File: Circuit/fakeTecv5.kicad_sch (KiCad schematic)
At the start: 76 parts, among them J1 EXTRA, J11 FET1 3,3, J12 FET2 3,3, J13 FET3 3,3, J14 GPS Pins, J16 Encoder Pads, J37 SCL, J38 JST-SH-4, J39 SDA, J40 3.3V, J41 GND, J42 FET1, J43 FET2, J44 FET3, J45 GND, J46 3.3V, J47 GND, J48 GND, J49 GND, J5 I2C Oled screen, J50 3.3V, J51 GND, J52 GND, J6 FET1 Drain, J7 FET2 Drain, J8 FET3 Drain, J9 JST-PH-2, M1 ERM Motor, Q1 AO3400A, Q2 AO3400A, Q3 AO3400A, SW1 Reset, SW2 SW_Push, SW3 RotaryEncoder_Switch, U1 XB8089D0, U2 HT-RA62, U3 nice!nano v2

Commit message: use alignment hole
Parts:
- U3: footprint faketec:NICE!NANO and pro-micro V2_2 SMD -> faketec:NICE!NANO and pro-micro V2_2 SMD_With_Alignment_Holes
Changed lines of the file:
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@@
 			)
 		)
-		(property "Footprint" "faketec:NICE!NANO and pro-micro V2_2 SMD"
+		(property "Footprint" "faketec:NICE!NANO and pro-micro V2_2 SMD_With_Alignment_Holes"
 			(at 124.46 82.55 0)
 			(effects

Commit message: adjust extra testpoint to the side of oled screen
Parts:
- J5: footprint Connector_PinHeader_2.54mm:PinHeader_1x04_P2.54mm_Vertical -> faketec:OLED_PinHeader_1x04_P2.54mm_Vertical
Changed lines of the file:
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@@
 			)
 		)
-		(property "Footprint" "Connector_PinHeader_2.54mm:PinHeader_1x04_P2.54mm_Vertical"
+		(property "Footprint" "faketec:OLED_PinHeader_1x04_P2.54mm_Vertical"
 			(at 179.07 30.48 0)
 			(effects

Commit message: hw: modify power connector to support both JST GH and PH connector
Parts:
- J9: footprint Connector_JST:JST_PH_S2B-PH-SM4-TB_1x02-1MP_P2.00mm_Horizontal -> faketec:JST_PH_S2B-PH-SM4-TB_1x02-1MP_P2.00mm_Horizontal
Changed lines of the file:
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@@
 			)
 		)
-		(property "Footprint" "Connector_JST:JST_PH_S2B-PH-SM4-TB_1x02-1MP_P2.00mm_Horizontal"
+		(property "Footprint" "faketec:JST_PH_S2B-PH-SM4-TB_1x02-1MP_P2.00mm_Horizontal"
 			(at 24.13 110.49 0)
 			(effects

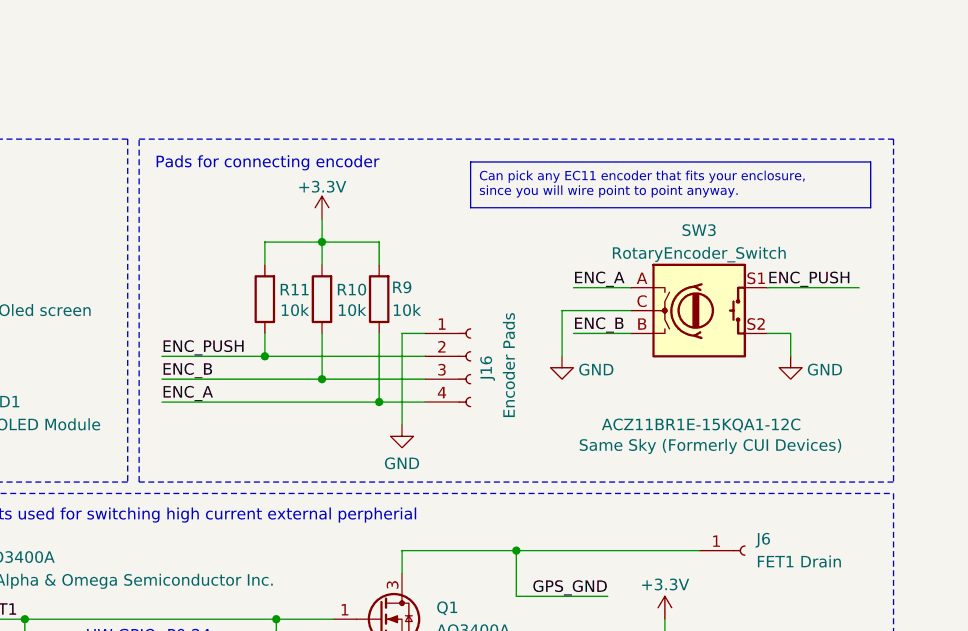
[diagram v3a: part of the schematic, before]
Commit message: hw: refactor spi routing. Make OLED screen pins friction fit
SPI is likely running under 50mHz mark so vias is not an issue and want to keep signal path small. Made careful note to keep all spi lines under the ground plane as much as possible.
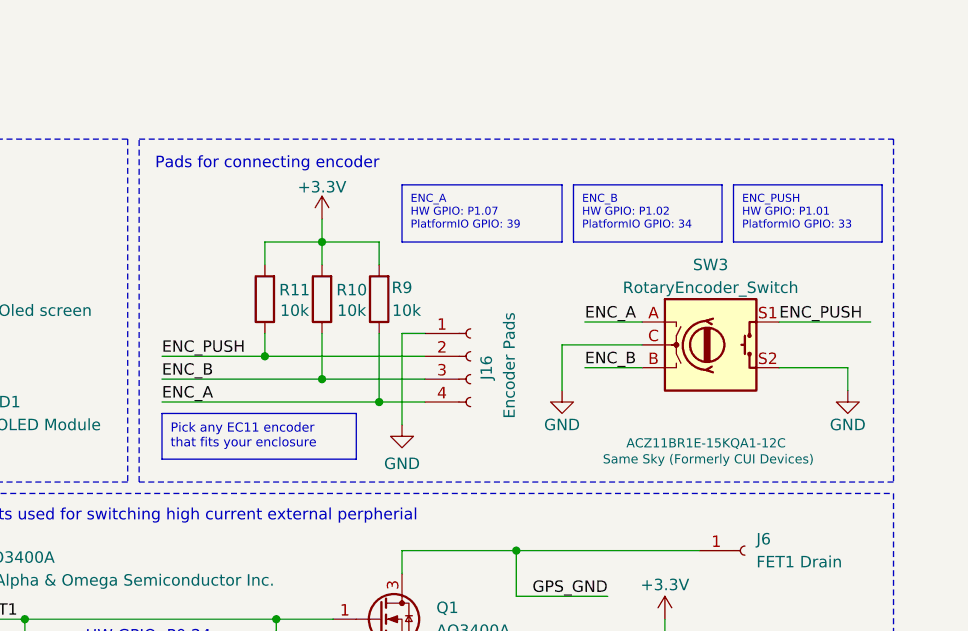
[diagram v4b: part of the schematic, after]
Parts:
- J5: footprint faketec:OLED_PinHeader_1x04_P2.54mm_Vertical -> faketec:OLED_PinHeader_1x04_P2.54mm_Vertical_Friction_Fit
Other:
- moved on the sheet: SW3
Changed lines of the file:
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@@
 		)
 	)
+	(text_box "ENC_B\nHW GPIO: P1.02\nPlatformIO GPIO: 34"
+		(exclude_from_sim no)
+		(at 247.65 19.05 0)
+		(size 16.51 6.35)
+		(margins 0.9525 0.9525 0.9525 0.9525)
+		(stroke
+			(width 0)
+			(type solid)
+		)
+		(fill
+			(type none)
+		)
+		(effects
+			(font
+				(size 0.889 0.889)
+			)
+			(justify left top)
+		)
+	)
+	(text_box "ENC_A\nHW GPIO: P1.07\nPlatformIO GPIO: 39"
+		(exclude_from_sim no)
+		(at 228.6 19.05 0)
+		(size 17.78 6.35)
+		(margins 0.9525 0.9525 0.9525 0.9525)
+		(stroke
+			(width 0)
+			(type solid)
+		)
+		(fill
+			(type none)
+		)
+		(effects
+			(font
+				(size 0.889 0.889)
+			)
+			(justify left top)
+		)
+	)
+	(text_box "ENC_PUSH\nHW GPIO: P1.01\nPlatformIO GPIO: 33"
+		(exclude_from_sim no)
+		(at 265.43 19.05 0)
+		(size 16.51 6.35)
+		(margins 0.9525 0.9525 0.9525 0.9525)
+		(stroke
+			(width 0)
+			(type solid)
+		)
+		(fill
+			(type none)
+		)
+		(effects
+			(font
+				(size 0.889 0.889)
+			)
+			(justify left top)
+		)
+	)
 	(text_box "Alternatively can use SI2312 (More expensive. Higher current)"
 		(exclude_from_sim no)
@@
 		)
 	)
-	(text_box "Can pick any EC11 encoder that fits your enclosure,\nsince you will wire point to point anyway."
+	(text_box "Pick any EC11 encoder that fits your enclosure"
 		(exclude_from_sim no)
-		(at 236.22 16.51 0)
-		(size 44.45 5.08)
+		(at 201.93 44.45 0)
+		(size 21.59 5.08)
 		(margins 0.9525 0.9525 0.9525 0.9525)
 		(stroke
@@
 	(wire
 		(pts
-			(xy 246.38 33.02) (xy 246.38 38.1)
+			(xy 246.38 36.83) (xy 246.38 41.91)
 		)
 		(stroke
@@
 	(wire
 		(pts
-			(xy 269.24 30.48) (xy 279.4 30.48)
+			(xy 270.51 34.29) (xy 280.67 34.29)
 		)
 		(stroke
@@
 	(wire
 		(pts
-			(xy 254 33.02) (xy 246.38 33.02)
+			(xy 255.27 36.83) (xy 246.38 36.83)
 		)
 		(stroke
@@
 	(wire
 		(pts
-			(xy 269.24 35.56) (xy 271.78 35.56)
+			(xy 270.51 39.37) (xy 278.13 39.37)
 		)
 		(stroke
@@
 	(wire
 		(pts
-			(xy 271.78 35.56) (xy 271.78 38.1)
+			(xy 278.13 39.37) (xy 278.13 41.91)
 		)
 		(stroke
@@
 	(wire
 		(pts
-			(xy 247.65 35.56) (xy 254 35.56)
+			(xy 248.92 39.37) (xy 255.27 39.37)
 		)
 		(stroke
@@
 	(wire
 		(pts
-			(xy 247.65 30.48) (xy 254 30.48)
+			(xy 248.92 34.29) (xy 255.27 34.29)
 		)
 		(stroke
@@
 	)
 	(label "ENC_A"
-		(at 247.65 30.48 0)
+		(at 248.92 34.29 0)
 		(effects
 			(font
@@
 	)
 	(label "ENC_PUSH"
-		(at 269.24 30.48 0)
+		(at 270.51 34.29 0)
 		(effects
 			(font
@@
 	)
 	(label "ENC_B"
-		(at 247.65 35.56 0)
+		(at 248.92 39.37 0)
 		(effects
 			(font
@@
 	(symbol
 		(lib_id "power:GND")
-		(at 246.38 38.1 0)
+		(at 246.38 41.91 0)
 		(unit 1)
 		(exclude_from_sim no)
@@
 		(dnp no)
 		(property "Reference" "#PWR09"
-			(at 246.38 44.45 0)
+			(at 246.38 48.26 0)
 			(effects
 				(font
@@
 		)
 		(property "Value" "GND"
-			(at 250.19 39.624 0)
+			(at 246.38 45.72 0)
 			(effects
 				(font
@@
 		)
 		(property "Footprint" ""
-			(at 246.38 38.1 0)
+			(at 246.38 41.91 0)
 			(effects
 				(font
@@
 		)
 		(property "Datasheet" ""
-			(at 246.38 38.1 0)
+			(at 246.38 41.91 0)
 			(effects
 				(font
@@
 		)
 		(property "Description" "Power symbol creates a global label with name \"GND\" , ground"
-			(at 246.38 38.1 0)
+			(at 246.38 41.91 0)
 			(effects
 				(font
@@
 	(symbol
 		(lib_id "Device:RotaryEncoder_Switch")
-		(at 261.62 33.02 0)
+		(at 262.89 36.83 0)
 		(unit 1)
 		(exclude_from_sim yes)
@@
 		(dnp no)
 		(property "Reference" "SW3"
-			(at 261.62 24.13 0)
+			(at 262.89 27.94 0)
 			(effects
 				(font
@@
 		)
 		(property "Value" "RotaryEncoder_Switch"
-			(at 261.62 26.67 0)
+			(at 262.89 30.48 0)
 			(effects
 				(font
@@
 		)
 		(property "Footprint" ""
-			(at 257.81 28.956 0)
+			(at 259.08 32.766 0)
 			(effects
 				(font
@@
 		)
 		(property "Datasheet" "https://www.cuidevices.com/product/resource/acz11.pdf"
-			(at 261.62 26.416 0)
+			(at 262.89 30.226 0)
 			(effects
 				(font
@@
 		)
 		(property "Description" "Rotary encoder, dual channel, incremental quadrate outputs, with switch"
-			(at 261.62 33.02 0)
+			(at 262.89 36.83 0)
 			(effects
 				(font
@@
 		)
 		(property "MPD" "EC11 horizontal rotary encoder Plum blossom shaft With switch 15/20mm 5PIN 20bit pulse digital potentiometer With knob cap"
-			(at 261.62 33.02 0)
+			(at 262.89 36.83 0)
 			(effects
 				(font
@@
 		)
 		(property "MPL" "https://www.aliexpress.com/item/1005010398201852.html or https://www.digikey.com.au/en/products/detail/same-sky-formerly-cui-devices/ACZ11BR1E-15KQA1-12C/1923334"
-			(at 261.62 33.02 0)
+			(at 262.89 36.83 0)
 			(effects
 				(font
@@
 		)
 		(property "Shopping" "https://www.aliexpress.com/w/wholesale-rotary-encoder-EC11-horizontal.html or https://www.digikey.com.au/short/7v5m7j9j"
-			(at 261.62 33.02 0)
+			(at 262.89 36.83 0)
 			(effects
 				(font
@@
 		)
 		(property "MPN" "ACZ11BR1E-15KQA1-12C"
-			(at 261.874 45.72 0)
+			(at 262.382 47.752 0)
 			(effects
 				(font
-					(size 1.27 1.27)
+					(size 1.016 1.016)
 				)
 			)
 		)
 		(property "Manufacturer" "Same Sky (Formerly CUI Devices)"
-			(at 262.89 48.006 0)
+			(at 262.636 49.53 0)
 			(effects
 				(font
-					(size 1.27 1.27)
+					(size 1.016 1.016)
 				)
 			)
 		)
 		(property "Package" "EC11"
-			(at 261.62 33.02 0)
+			(at 262.89 36.83 0)
 			(effects
 				(font
@@
 	(symbol
 		(lib_id "power:GND")
-		(at 271.78 38.1 0)
+		(at 278.13 41.91 0)
 		(unit 1)
 		(exclude_from_sim no)
@@
 		(dnp no)
 		(property "Reference" "#PWR047"
-			(at 271.78 44.45 0)
+			(at 278.13 48.26 0)
 			(effects
 				(font
@@
 		)
 		(property "Value" "GND"
-			(at 275.59 39.624 0)
+			(at 278.13 45.72 0)
 			(effects
 				(font
@@
 		)
 		(property "Footprint" ""
-			(at 271.78 38.1 0)
+			(at 278.13 41.91 0)
 			(effects
 				(font
@@
 		)
 		(property "Datasheet" ""
-			(at 271.78 38.1 0)
+			(at 278.13 41.91 0)
 			(effects
 				(font
@@
 		)
 		(property "Description" "Power symbol creates a global label with name \"GND\" , ground"
-			(at 271.78 38.1 0)
+			(at 278.13 41.91 0)
 			(effects
 				(font
@@
 			)
 		)
-		(property "Footprint" "faketec:OLED_PinHeader_1x04_P2.54mm_Vertical"
+		(property "Footprint" "faketec:OLED_PinHeader_1x04_P2.54mm_Vertical_Friction_Fit"
 			(at 179.07 30.48 0)
 			(effects

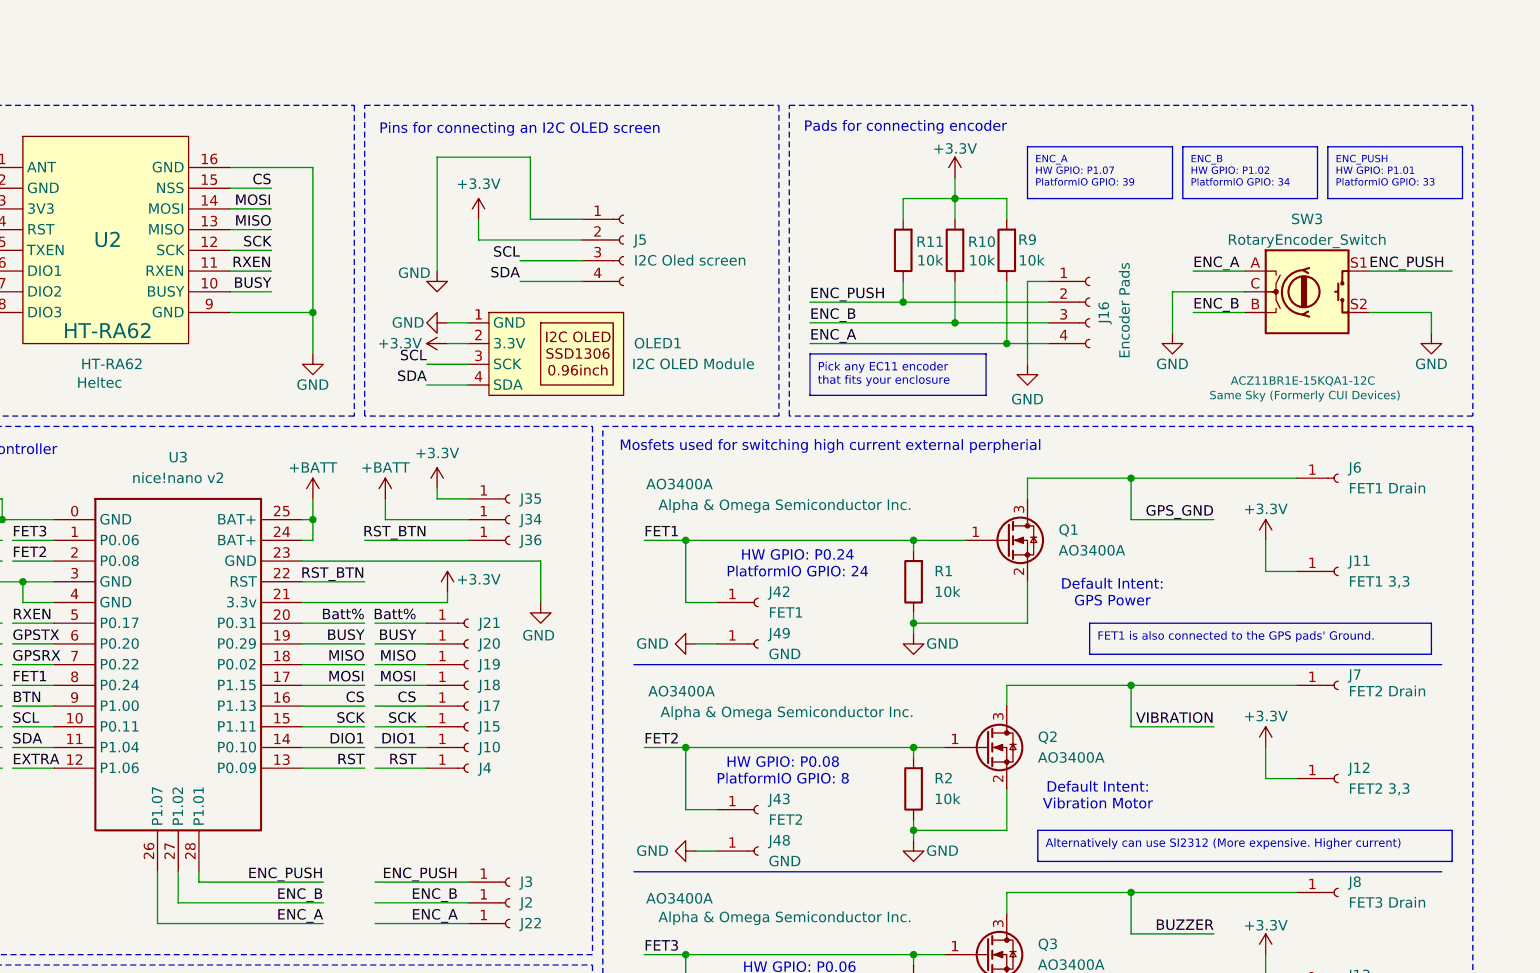
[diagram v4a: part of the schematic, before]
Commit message: hw: fix incorrect label on nice!nano symbol and adjust schematic.
This effects the encoder controls. No change to pcb required.
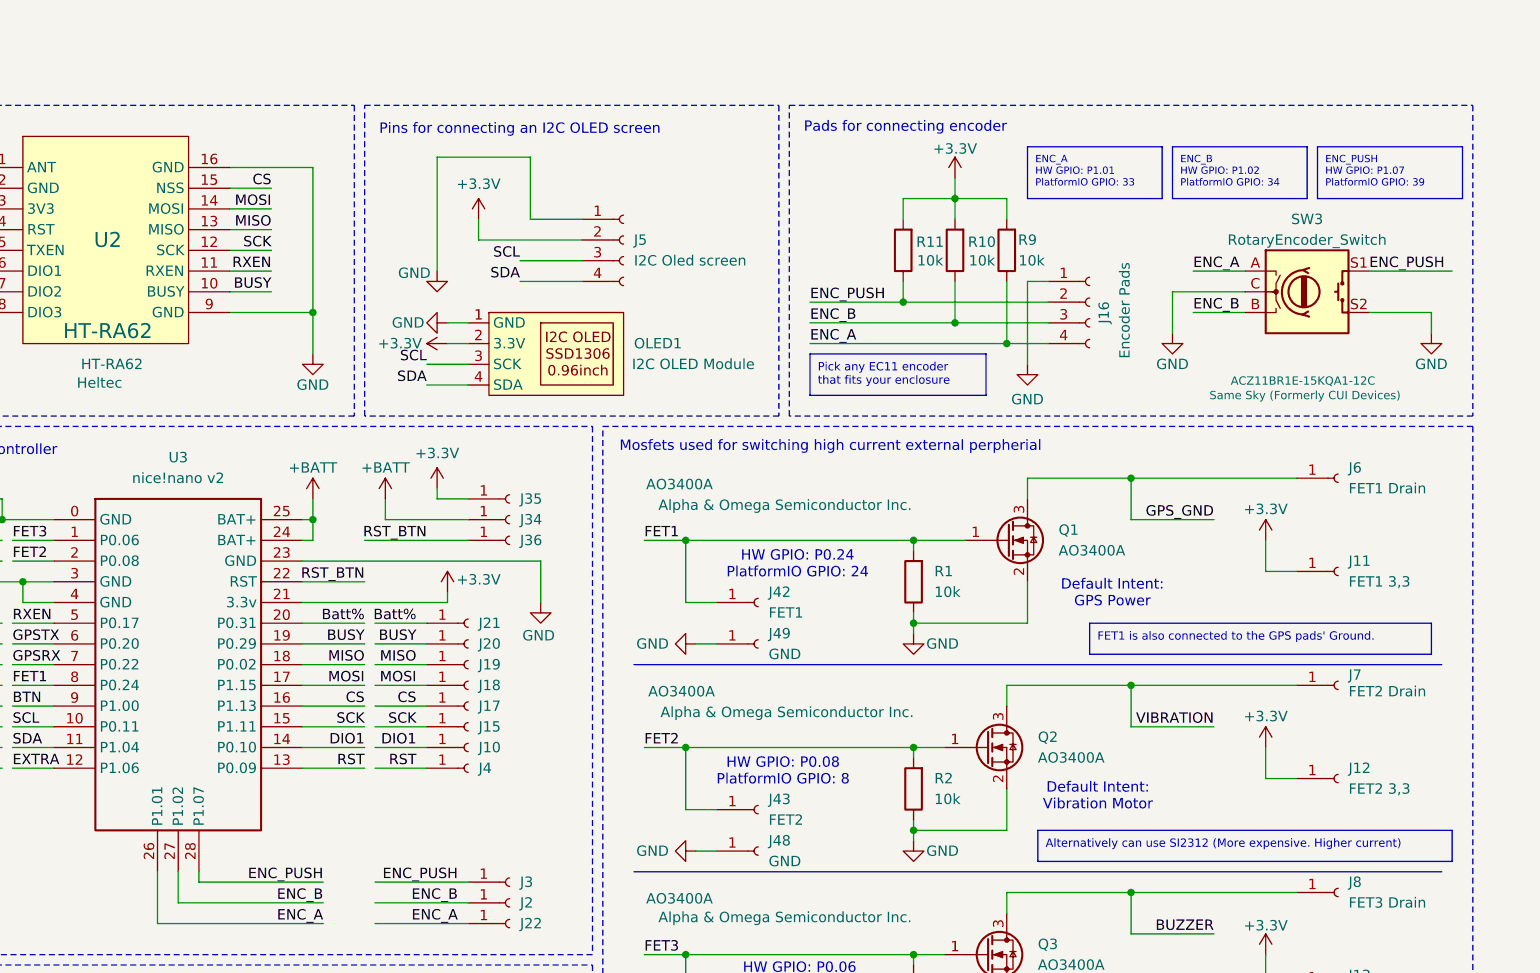
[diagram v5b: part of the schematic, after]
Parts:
- U3: symbol Nice_Nano:nice!nano v2 -> faketec:nice!nano_v2
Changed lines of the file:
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@@
 	(text_box "ENC_B\nHW GPIO: P1.02\nPlatformIO GPIO: 34"
 		(exclude_from_sim no)
-		(at 247.65 19.05 0)
+		(at 246.38 19.05 0)
 		(size 16.51 6.35)
 		(margins 0.9525 0.9525 0.9525 0.9525)
@@
 		)
 	)
-	(text_box "ENC_A\nHW GPIO: P1.07\nPlatformIO GPIO: 39"
+	(text_box "ENC_PUSH\nHW GPIO: P1.07\nPlatformIO GPIO: 39"
 		(exclude_from_sim no)
-		(at 228.6 19.05 0)
+		(at 264.16 19.05 0)
 		(size 17.78 6.35)
 		(margins 0.9525 0.9525 0.9525 0.9525)
@@
 		)
 	)
-	(text_box "ENC_PUSH\nHW GPIO: P1.01\nPlatformIO GPIO: 33"
+	(text_box "ENC_A\nHW GPIO: P1.01\nPlatformIO GPIO: 33"
 		(exclude_from_sim no)
-		(at 265.43 19.05 0)
+		(at 228.6 19.05 0)
 		(size 16.51 6.35)
 		(margins 0.9525 0.9525 0.9525 0.9525)
@@
 	)
 	(symbol
-		(lib_id "Nice_Nano:nice!nano v2")
+		(lib_id "faketec:nice!nano_v2")
 		(at 124.46 82.55 0)
 		(unit 1)
